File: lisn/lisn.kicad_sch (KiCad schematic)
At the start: 33 parts, among them J1 IN+, J2 IN-, J3 GND, J4 GND, J5 OUT+, J6 OUT-, J7 SMA, SW1 DPDT, T1 SWB2010

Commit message: Update LISN PCB
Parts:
- added R9: 68, Resistor_SMD:R_0603_1608Metric, symbol Device:R
- R5, R6: value 50 -> 82
- R7: value 18 -> 30
- R8: value 82 -> 68
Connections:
- net GND: now also R8.2, R9.2; no longer R8.1
- net at D1.1 (K), D2.2 (A), R1.2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: now also R9.1
- net at D5.2 (A), D6.1 (K), J7.1 (In)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: no longer R8.2
- net at D3.1 (K), D4.2 (A), R3.2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: now also R8.1
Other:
- note added: "Impedance at transformer: 41 ohm common-mode, 82 ohm differential."
- company: (none) -> Petteri Aimonen
- title: (none) -> 50 ohm LISN

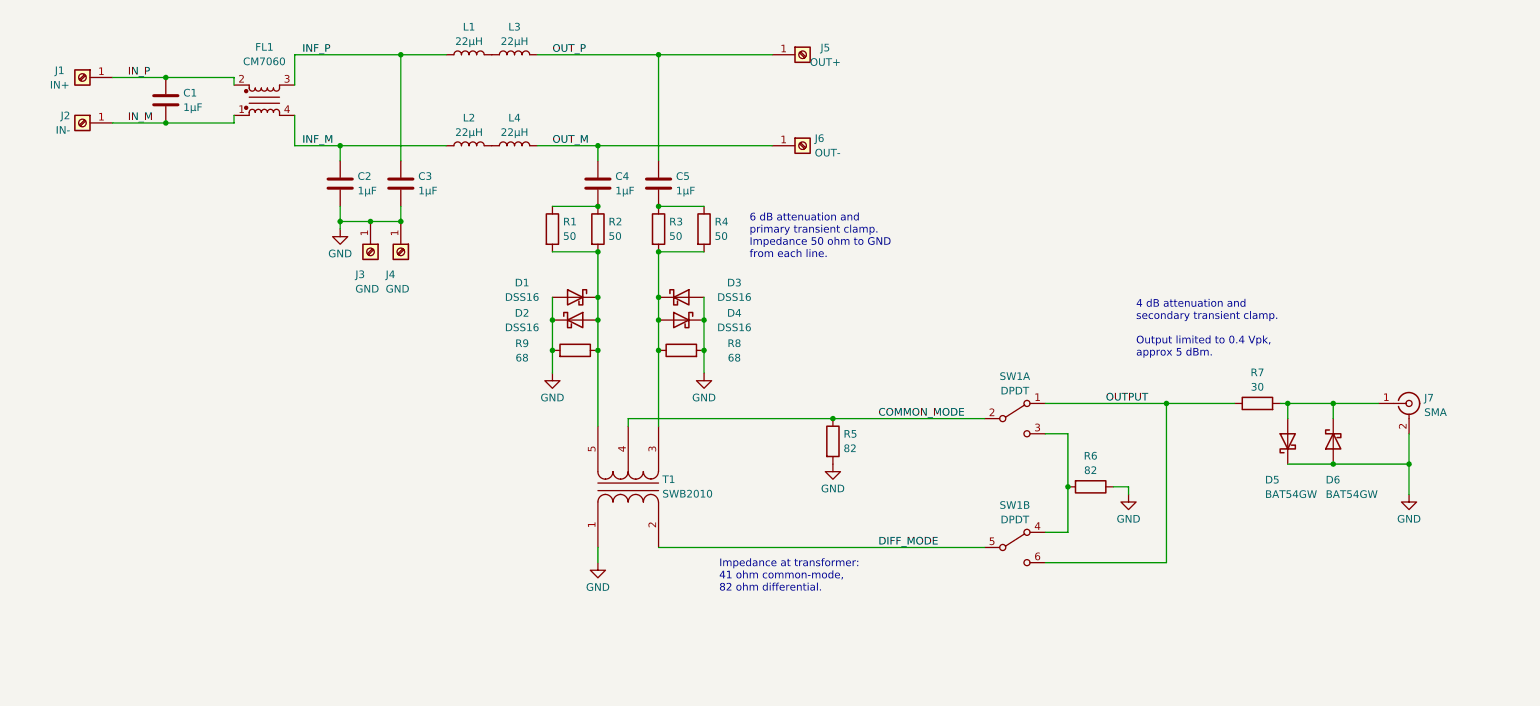
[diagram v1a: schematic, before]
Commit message: Add parametric FreeCAD design, add README.
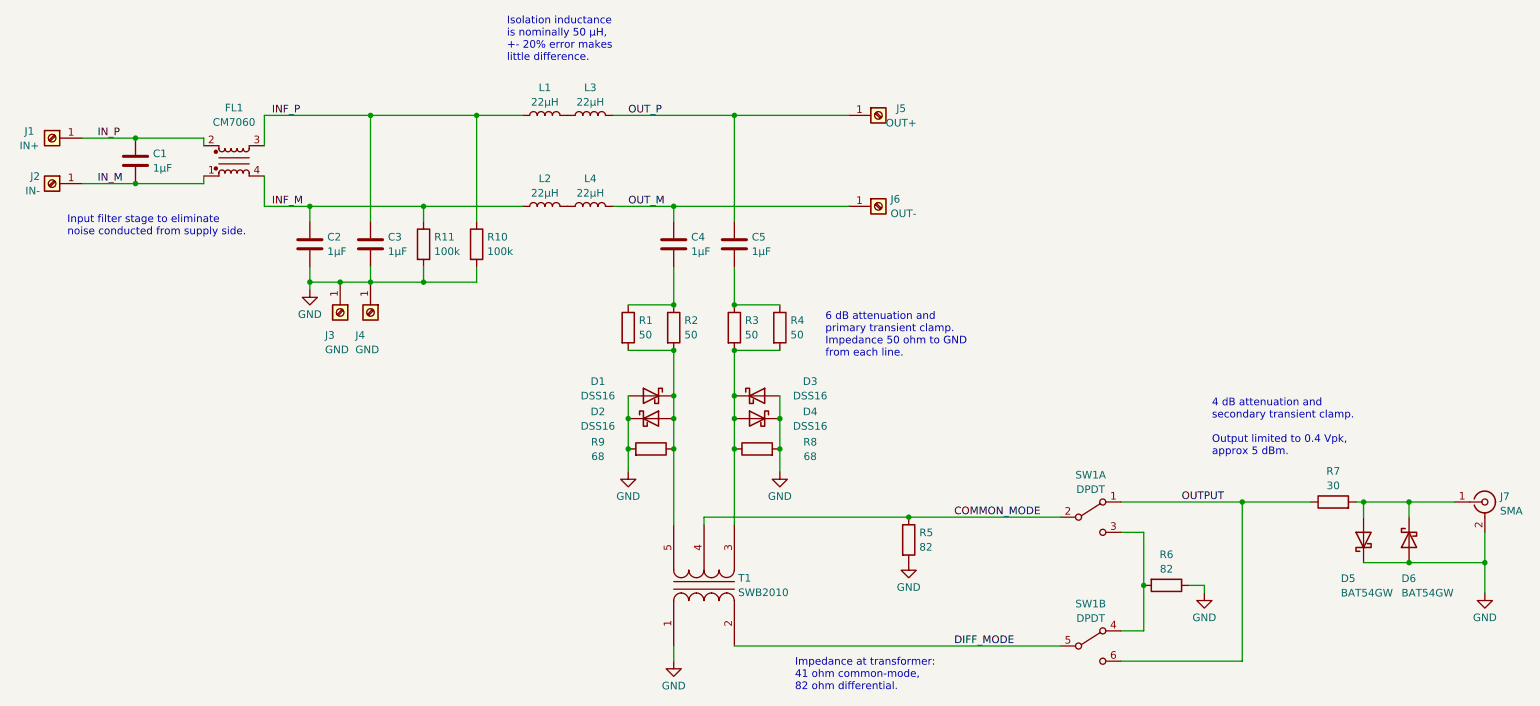
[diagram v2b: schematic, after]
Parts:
- added R10, R11: 100k, Resistor_SMD:R_0603_1608Metric, symbol Device:R
- C1, C2, C3, C4, C5: Notes (none) -> 100 V 1µF 1210 X7R ceramic capacitor; PartNumber (none) -> C1210J105K1RAC7800
- D1, D2, D3, D4: Notes (none) -> SOD123 schottky diode, > 2A pulse current capability; PartNumber (none) -> DSS16U
- D5, D6: Notes (none) -> SOD123 schottky diode, low forward voltage; PartNumber (none) -> BAT54GW
- FL1: Notes (none) -> Common mode choke; PartNumber (none) -> CM7060M132R-10
- J1, J2: Notes (none) -> Banana connector, soldered to PCB and screwed into enclosure; PartNumber (none) -> 108-0902-001
- J3, J4: Notes (none) -> Mounting screws and ground connection
- J5: Notes (none) -> Binding post for power output; PartNumber (none) -> CL1572
- J6: Notes (none) -> Binding post for power output; PartNumber (none) -> CL1575
- J7: Notes (none) -> Edge mount SMA connector; PartNumber (none) -> RF2-145A-T-17-50-G-HDW
- L1, L2, L3, L4: Notes (none) -> 22µH to 27µH inductor, high saturation current; PartNumber (none) -> SDR0805-220ML
- R1, R2, R3, R4, R5, R6, R7, R8, R9: Notes (none) -> Generic 0603 1% resistor
- SW1: Notes (none) -> Slide switch for output mode selection; PartNumber (none) -> JS202011JCQN
- T1: Notes (none) -> SWB1010-SMLD and SWB3010-SMLD are compatible; PartNumber (none) -> SWB2010-SMLD
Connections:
- net GND: now also R10.2, R11.2
- net INF_M: now also R11.1
- net INF_P: now also R10.1
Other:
- note added: "Input filter stage to eliminate noise conducted from supply side."
- note added: "Isolation inductance is nominally 50 µH, +- 20% error makes little difference."
- title: 50 ohm LISN -> LISN (50 µH, 50 ohm, 10 dB attenuation)
- moved on the sheet: C1, C2, C3, C4, C5, D1, D2, D3, D4, D5, D6, FL1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
